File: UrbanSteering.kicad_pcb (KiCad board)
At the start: 2 copper layers, 144 x 100 mm, 49 parts, among them J1 Joystick, J2 Main_conn, J3 CAN_term, J4 STM32L432, J5 Screen_Left, J6 Screen_Right, J9 Proximity_sensor, U1 MCP2562, U2 74HC595PW, U3 74HC597D

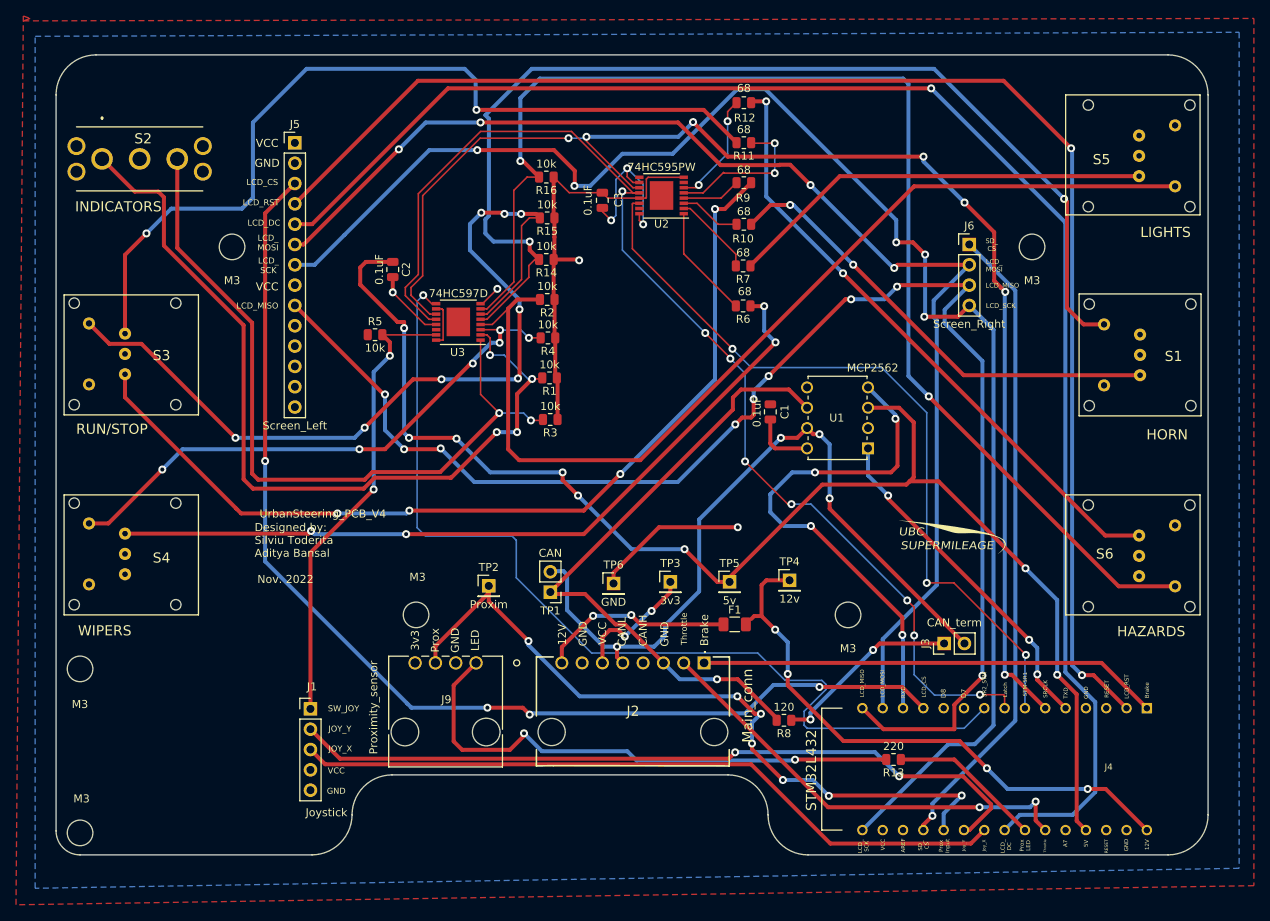
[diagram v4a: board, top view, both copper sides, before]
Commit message: made capacitor and stm shifting change, also edited main connector labels
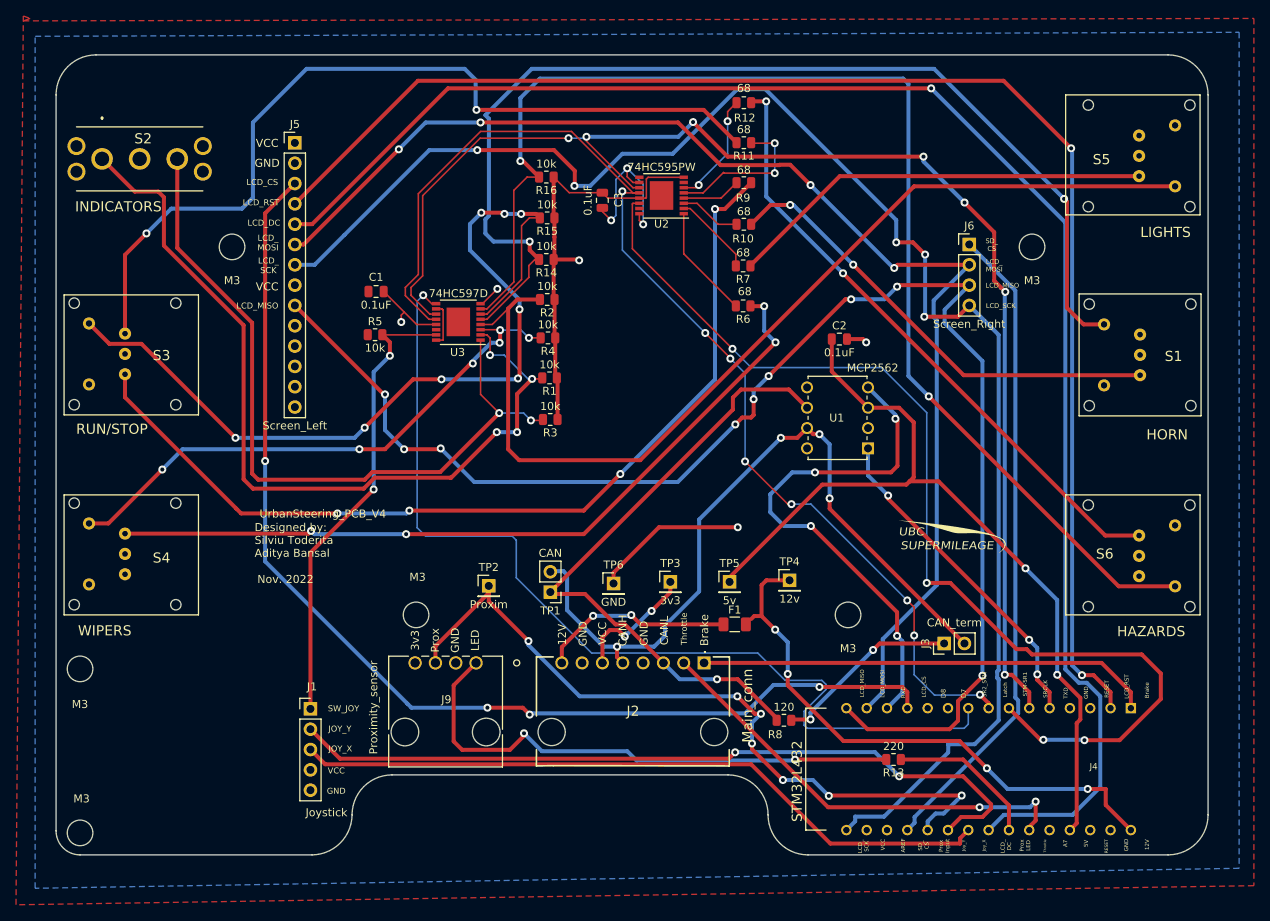
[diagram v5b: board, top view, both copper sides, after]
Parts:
- moved C2 56.5 mm to (197.9, 85.5), turned to 0 degrees
- moved C1 51.5 mm to (140.0, 79.6), turned to 0 degrees
- moved J4 2.00 mm to (228.0, 139.3)
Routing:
- net +5V: track 173.7 -> 107.7 mm, vias 8 -> 2
- net /STM-SR1: track 95.9 -> 133.0 mm, vias 3 -> 4
- net GND: track 92.5 -> 87.9 mm, vias 4 -> 5
- net /LCD_SCK: track 192.5 -> 196.2 mm
- net /LCD_DC: track 196.3 -> 199.4 mm
- net /Latch: track 146.0 -> 143.4 mm
- net /JoystickY: track 94.7 -> 96.7 mm
- net /LCD_MISO: track 180.9 -> 182.5 mm
- net /JoystickX: track 89.8 -> 88.2 mm
- net /ProximInput: track 93.3 -> 94.7 mm
- net /SD_CS: track 80.3 -> 81.5 mm, vias 1 -> 0
- net /LCD_MOSI: track 158.6 -> 159.4 mm
- net Net-(J2-Pad1): track 57.7 -> 56.9 mm
- net /TXD: track 42.7 -> 41.9 mm
- net /SRCLK: track 170.8 -> 169.9 mm
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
